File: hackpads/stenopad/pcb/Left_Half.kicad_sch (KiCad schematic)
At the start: 24 parts, among them SW1 SW_Push, SW10 SW_Push, SW11 SW_Push, SW2 SW_Push, SW3 SW_Push, SW4 SW_Push, SW5 SW_Push, SW6 SW_Push, SW7 SW_Push, SW8 SW_Push, SW9 SW_Push, U1 Seeed_XIAO_RP2040, U2 MCP23008-xSO

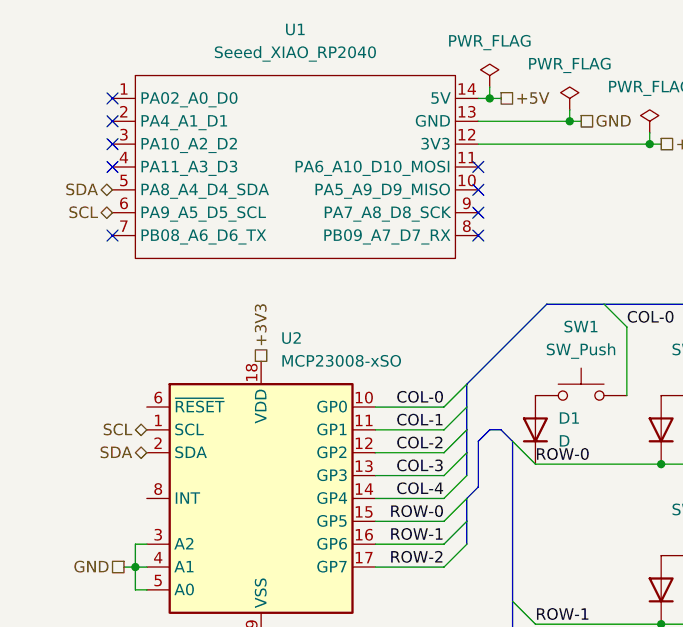
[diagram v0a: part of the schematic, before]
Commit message: Add most of the wiring for the StenoPad coprocessor to the schematic
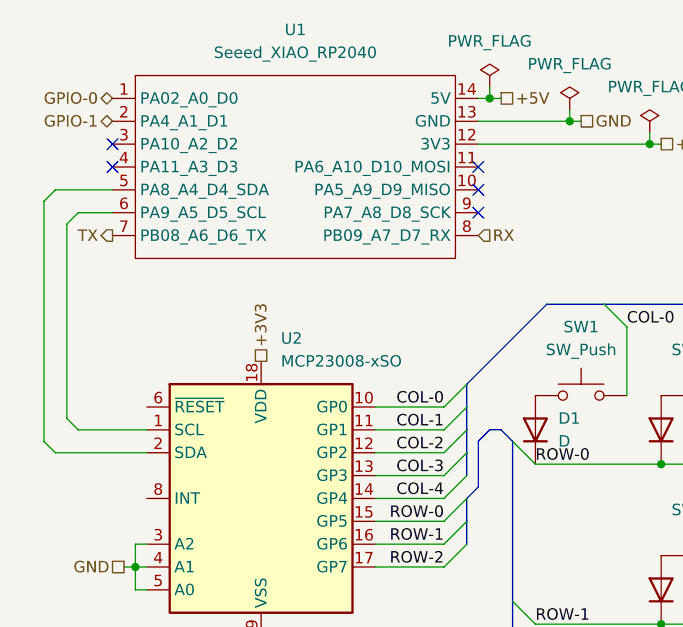
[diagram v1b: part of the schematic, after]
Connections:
- net GPIO-0: now reaches U1.1 (PA02_A0_D0)
- net GPIO-1: now reaches U1.2 (PA4_A1_D1)
- net TX: now reaches U1.7 (PB08_A6_D6_TX)
- net RX: now reaches U1.8 (PB09_A7_D7_RX)
- net SCL: no longer names the net of U1.6 (PA9_A5_D5_SCL), U2.1 (SCL)
- net SDA: no longer names the net of U1.5 (PA8_A4_D4_SDA), U2.2 (SDA)
- no-connect marks 9 -> 5
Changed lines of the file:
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@@
-	)
-	(no_connect
-		(at 64.77 40.64)
 	)
 	(no_connect
@@
 	)
 	(no_connect
-		(at 24.13 25.4)
-	)
-	(no_connect
 		(at 24.13 30.48)
-	)
-	(no_connect
-		(at 24.13 27.94)
-	)
-	(no_connect
-		(at 24.13 40.64)
 	)
 	(no_connect
@@
 	(wire
 		(pts
+			(xy 20.32 38.1) (xy 19.05 39.37)
+		)
+		(stroke
+			(width 0)
+			(type default)
+		)
+	)
+	(wire
+		(pts
 			(xy 74.93 26.67) (xy 74.93 27.94)
 		)
@@
 	(wire
 		(pts
+			(xy 19.05 39.37) (xy 19.05 60.96)
+		)
+		(stroke
+			(width 0)
+			(type default)
+		)
+	)
+	(wire
+		(pts
 			(xy 99.06 83.82) (xy 113.03 83.82)
 		)
@@
 	(wire
 		(pts
+			(xy 17.78 35.56) (xy 24.13 35.56)
+		)
+		(stroke
+			(width 0)
+			(type default)
+		)
+	)
+	(wire
+		(pts
+			(xy 16.51 36.83) (xy 16.51 63.5)
+		)
+		(stroke
+			(width 0)
+			(type default)
+		)
+	)
+	(wire
+		(pts
 			(xy 85.09 30.48) (xy 83.82 30.48)
 		)
@@
 	(wire
 		(pts
+			(xy 24.13 38.1) (xy 20.32 38.1)
+		)
+		(stroke
+			(width 0)
+			(type default)
+		)
+	)
+	(wire
+		(pts
 			(xy 53.34 67.31) (xy 60.96 67.31)
 		)
@@
 	(wire
 		(pts
+			(xy 20.32 62.23) (xy 27.94 62.23)
+		)
+		(stroke
+			(width 0)
+			(type default)
+		)
+	)
+	(wire
+		(pts
 			(xy 26.67 77.47) (xy 26.67 80.01)
 		)
@@
 		)
 	)
+	(wire
+		(pts
+			(xy 17.78 64.77) (xy 27.94 64.77)
+		)
+		(stroke
+			(width 0)
+			(type default)
+		)
+	)
 	(bus
 		(pts
@@
 	(wire
 		(pts
+			(xy 16.51 63.5) (xy 17.78 64.77)
+		)
+		(stroke
+			(width 0)
+			(type default)
+		)
+	)
+	(wire
+		(pts
 			(xy 53.34 72.39) (xy 60.96 72.39)
 		)
@@
 	(wire
 		(pts
+			(xy 17.78 35.56) (xy 16.51 36.83)
+		)
+		(stroke
+			(width 0)
+			(type default)
+		)
+	)
+	(wire
+		(pts
 			(xy 95.25 58.42) (xy 95.25 76.2)
 		)
@@
 		(pts
 			(xy 85.09 66.04) (xy 99.06 66.04)
+		)
+		(stroke
+			(width 0)
+			(type default)
+		)
+	)
+	(wire
+		(pts
+			(xy 19.05 60.96) (xy 20.32 62.23)
 		)
 		(stroke
@@
 		)
 	)
-	(hierarchical_label "SDA"
+	(hierarchical_label "GPIO-1"
 		(shape bidirectional)
-		(at 24.13 35.56 180)
+		(at 24.13 27.94 180)
 		(fields_autoplaced yes)
 		(effects
@@
 		)
 	)
-	(hierarchical_label "SCL"
+	(hierarchical_label "GPIO-0"
 		(shape bidirectional)
-		(at 24.13 38.1 180)
+		(at 24.13 25.4 180)
 		(fields_autoplaced yes)
 		(effects
@@
 		)
 	)
-	(hierarchical_label "SCL"
-		(shape bidirectional)
-		(at 27.94 62.23 180)
-		(fields_autoplaced yes)
-		(effects
-			(font
-				(size 1.27 1.27)
-			)
-			(justify right)
-		)
-	)
-	(hierarchical_label "SDA"
-		(shape bidirectional)
-		(at 27.94 64.77 180)
-		(fields_autoplaced yes)
-		(effects
-			(font
-				(size 1.27 1.27)
-			)
-			(justify right)
+	(hierarchical_label "RX"
+		(shape input)
+		(at 64.77 40.64 0)
+		(fields_autoplaced yes)
+		(effects
+			(font
+				(size 1.27 1.27)
+			)
+			(justify left)
 		)
 	)
@@
 		(fields_autoplaced yes)
 		(effects
+			(font
+				(size 1.27 1.27)
+			)
+			(justify right)
+		)
+	)
+	(hierarchical_label "TX"
+		(shape output)
+		(at 24.13 40.64 180)
+		(fields_autoplaced yes)
+		(effects
